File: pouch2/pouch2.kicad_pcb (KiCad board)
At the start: 2 copper layers, 80 x 100 mm, 161 parts, among them J101 Conn_01x06_Male, J102 Conn_01x03_Male, J103 Conn_01x04_Male, J501 Conn_01x02_Male, J502 Conn_01x02_Male, J503 Conn_01x02_Male, J504 Conn_01x02_Male, J505 Conn_02x02_Odd_Even, J701 PiZero, J901 Conn_02x03_Counter_Clockwise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

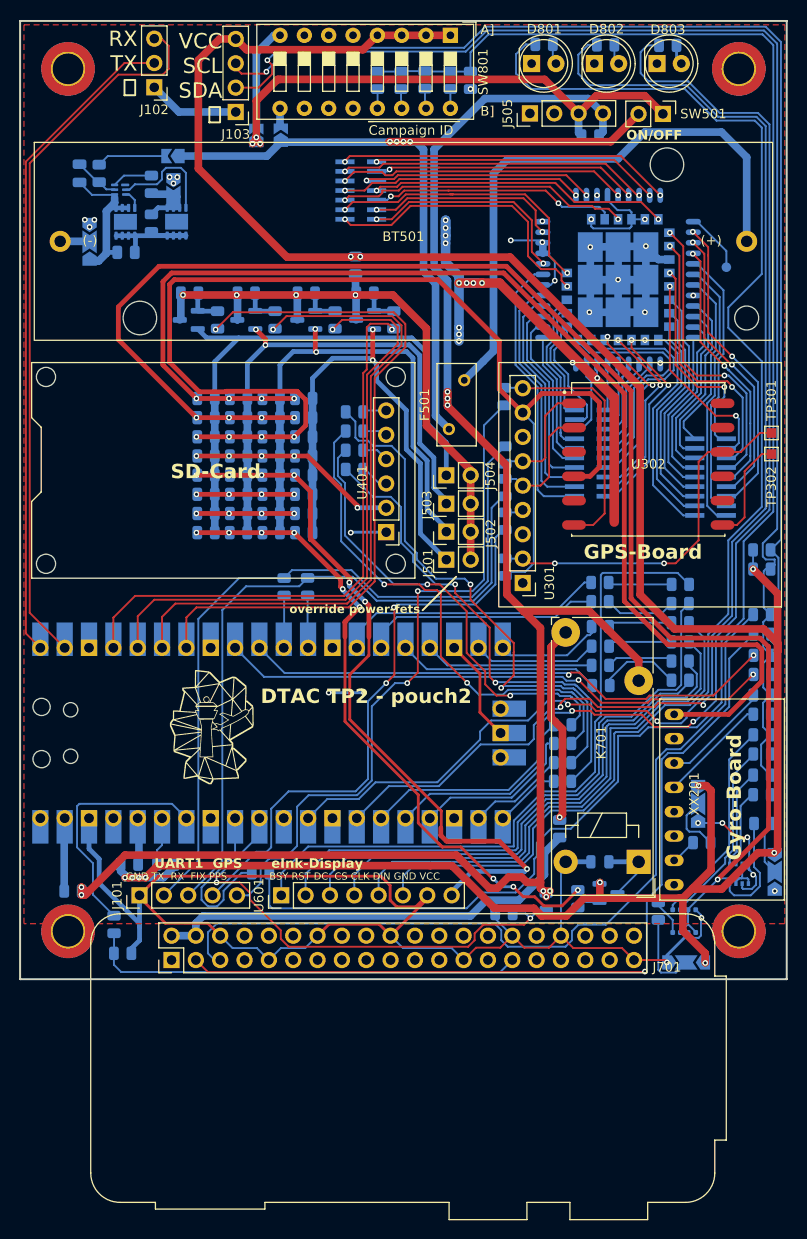
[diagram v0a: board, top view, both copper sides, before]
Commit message: added VCC-battery measurement line
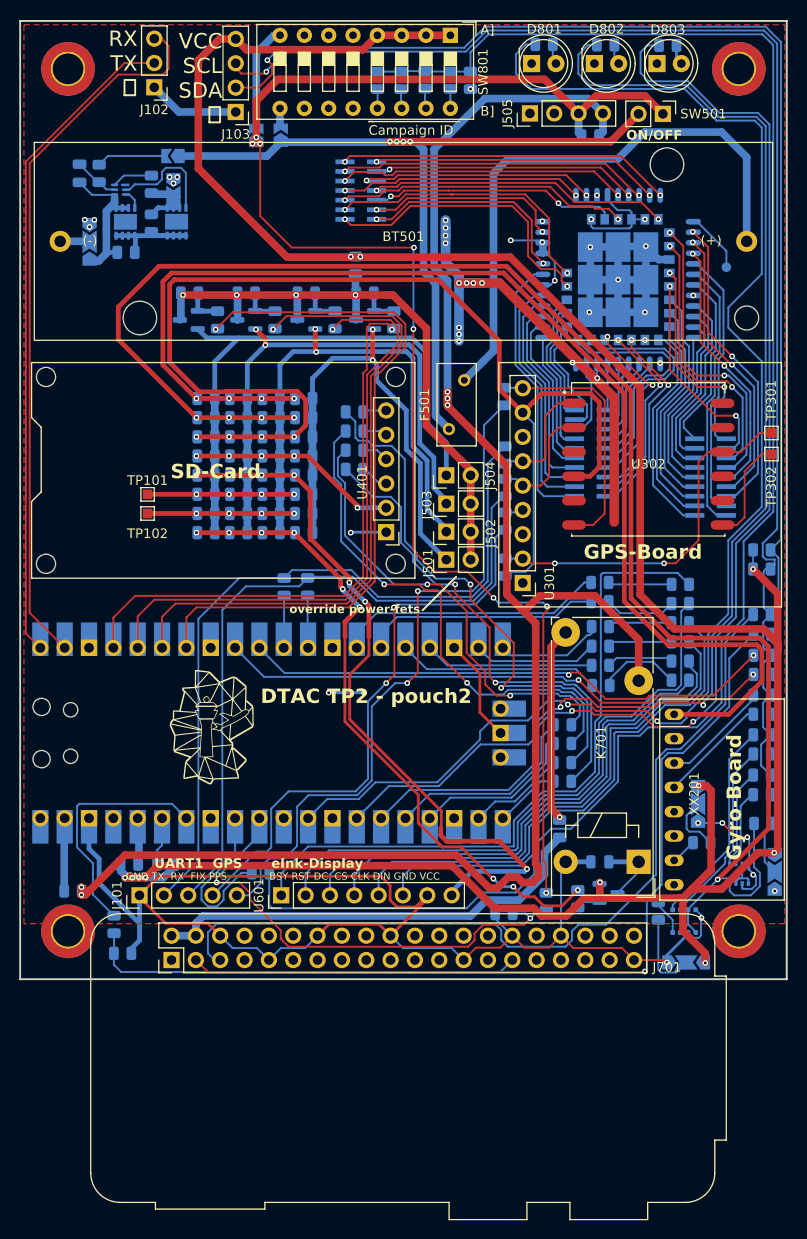
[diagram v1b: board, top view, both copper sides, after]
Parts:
- added TP101: TestPoint, TestPoint:TestPoint_Pad_1.0x1.0mm, F.Cu at (63.3, 99.4)
- added TP102: TestPoint, TestPoint:TestPoint_Pad_1.0x1.0mm, F.Cu at (63.3, 101.4)
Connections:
- J505 pad 3: /Power/VCC_ANTE_BOOST -> VCC_ANTE_BOOST
- JP502 pad 1: /Power/VCC_ANTE_BOOST -> VCC_ANTE_BOOST
- R116 pad 1: VCC -> VCC_ANTE_BOOST
- R542 pad 2: /Power/VCC_ANTE_BOOST -> VCC_ANTE_BOOST
- SW501 pad 1: /Power/VCC_ANTE_BOOST -> VCC_ANTE_BOOST
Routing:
- net VCC_ANTE_BOOST: track 0.00 -> 157.5 mm, vias 0 -> 8
- net /Power/VCC_ANTE_BOOST: track 54.2 -> 0.00 mm, vias 3 -> 0
- net /VCC_S7: track 10.2 -> 15.3 mm
- net /VCC_S6: track 10.2 -> 15.3 mm
- net VCC: track 178.8 -> 178.5 mm, vias 8 -> 5
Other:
- board text added: "SPI0"
- board text added: "SPI1"

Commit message: rev1
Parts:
- G***: moved to B.Cu
- moved G*** 22.0 mm to (91.8, 124.1), turned to 180 degrees
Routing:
- net GND: track 304.1 -> 318.8 mm, vias 44 -> 46
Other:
- board text added: "DTAC TPA AP5"
- board text added: "S1 Env/BME S2 Gyro/MPU S3 GPS S4 SD S5 Display S6 n.c. (TP101) S7 n.c. (TP102) S8 Pi Zero"
- board text added: "UART1| GPS"
- board text added: "pouch2 rev 1.0 2024-10-01"
- board text removed: "DTAC TP2 - pouch2"
- board text removed: "UART1 GPS"

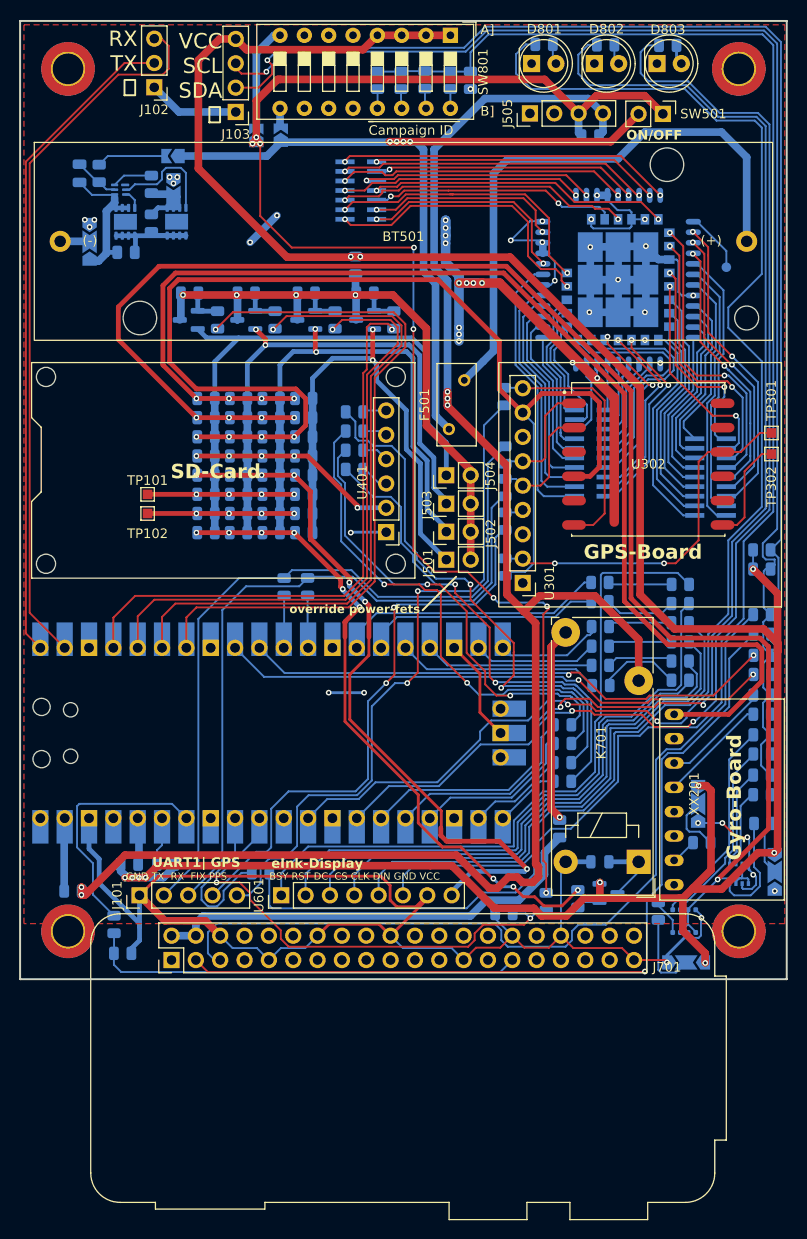
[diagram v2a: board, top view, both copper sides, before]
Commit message: moved all holes on pads away
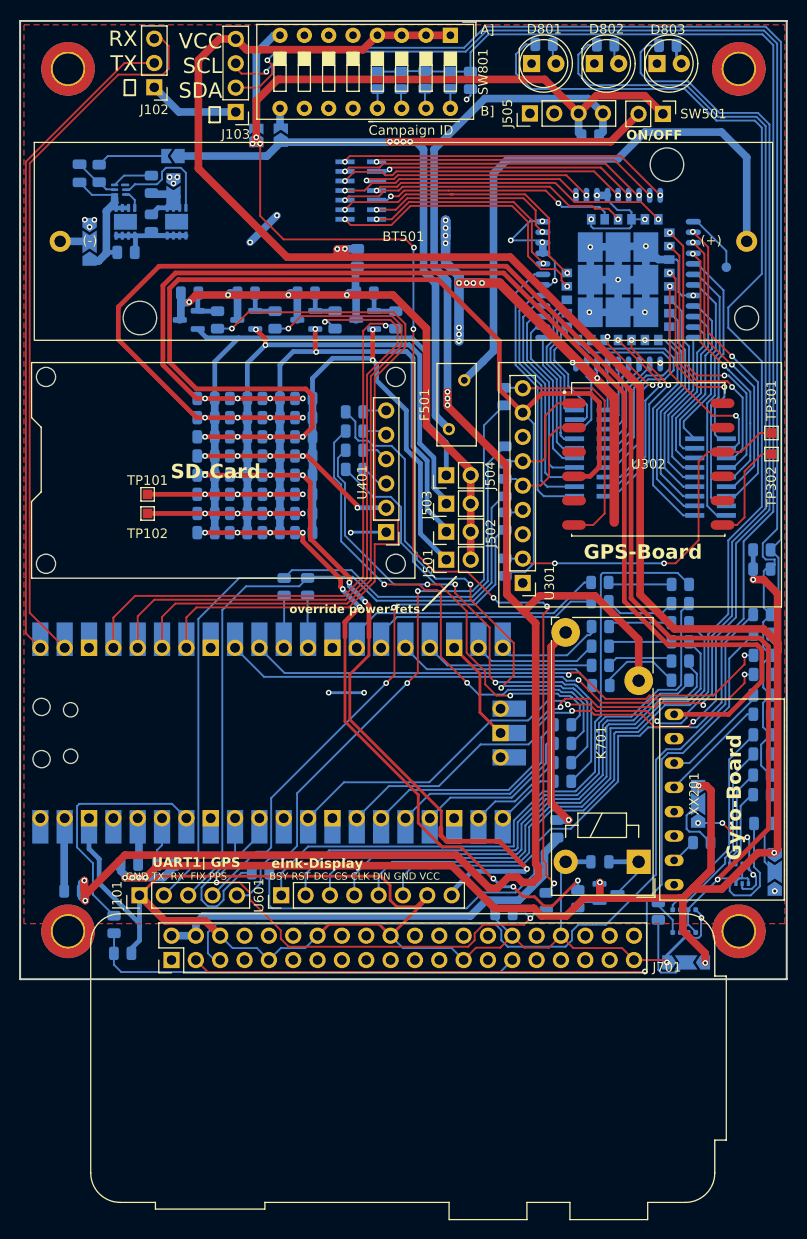
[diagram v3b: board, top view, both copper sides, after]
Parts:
- moved R509 0.82 mm to (85.2, 74.7)
- moved R702 0.30 mm to (106.0, 134.3)
- moved R501 0.20 mm to (89.2, 81.2)
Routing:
- net /SW_VCC4: track 73.6 -> 78.3 mm
- net /VCC_S8: track 68.6 -> 72.9 mm
- net /VCC_S7: track 15.3 -> 19.5 mm
- net /VCC_S6: track 15.3 -> 19.5 mm
- net /VCC_S1: track 129.3 -> 133.5 mm
- net /VCC_S2: track 164.5 -> 168.6 mm
- net /GPS_FIX: track 60.3 -> 56.2 mm
- net /VCC_S3: track 122.2 -> 126.3 mm
- net /GPS_PPS: track 71.4 -> 67.7 mm
- net VCC: track 178.5 -> 182.2 mm
- net /Power/VPOW: track 66.0 -> 69.5 mm
- net +3.3V: track 273.3 -> 276.8 mm
- net /VCC_S5: track 75.2 -> 78.1 mm
- net /VCC_S4: track 22.1 -> 24.5 mm
- net /SW_VCC2: track 63.9 -> 65.8 mm
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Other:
- board text added: "pouch2 rev 1.1 2024-10-09"
- board text removed: "pouch2 rev 1.0 2024-10-01"
